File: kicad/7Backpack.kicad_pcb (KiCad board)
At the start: 2 copper layers, 14 x 83.2 mm, 14 parts, among them J1 Conn_01x06, J2 Conn_01x06, U1 TPIC6C596PWR, U2 15101BS-30101BS

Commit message: AddedGerber files
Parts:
- R9: value 30Ω ? -> 2kΩ
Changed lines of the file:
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@@
       (layerselection 0x00010fc_ffffffff)
       (disableapertmacros false)
-      (usegerberextensions false)
+      (usegerberextensions true)
       (usegerberattributes true)
       (usegerberadvancedattributes true)
-      (creategerberjobfile true)
+      (creategerberjobfile false)
       (svguseinch false)
       (svgprecision 6)
@@
       (psa4output false)
       (plotreference true)
-      (plotvalue true)
+      (plotvalue false)
       (plotinvisibletext false)
       (sketchpadsonfab false)
-      (subtractmaskfromsilk false)
+      (subtractmaskfromsilk true)
       (outputformat 1)
       (mirror false)
-      (drillshape 1)
+      (drillshape 0)
       (scaleselection 1)
-      (outputdirectory "Gerber/")
+      (outputdirectory "../Gerber/")
     )
   )
@@
     (descr "Resistor SMD 0603 (1608 Metric), square (rectangular) end terminal, IPC_7351 nominal, (Body size source: IPC-SM-782 page 72, https://www.pcb-3d.com/wordpress/wp-content/uploads/ipc-sm-782a_amendment_1_and_2.pdf), generated with kicad-footprint-generator")
     (tags "resistor")
+    (property "LCSC" "C22810")
     (property "Sheetfile" "7Backpack.kicad_sch")
     (property "Sheetname" "")
@@
     (descr "Resistor SMD 0603 (1608 Metric), square (rectangular) end terminal, IPC_7351 nominal, (Body size source: IPC-SM-782 page 72, https://www.pcb-3d.com/wordpress/wp-content/uploads/ipc-sm-782a_amendment_1_and_2.pdf), generated with kicad-footprint-generator")
     (tags "resistor")
+    (property "LCSC" "C22975")
     (property "Sheetfile" "7Backpack.kicad_sch")
     (property "Sheetname" "")
@@
       (effects (font (size 1 1) (thickness 0.15)))
     )
-    (fp_text value "30Ω ?" (at 0 1.43 90) (layer "F.Fab")
+    (fp_text value "2kΩ" (at 0 1.43 90) (layer "F.Fab")
       (effects (font (size 1 1) (thickness 0.15)))
     )
@@
     (descr "Resistor SMD 0603 (1608 Metric), square (rectangular) end terminal, IPC_7351 nominal, (Body size source: IPC-SM-782 page 72, https://www.pcb-3d.com/wordpress/wp-content/uploads/ipc-sm-782a_amendment_1_and_2.pdf), generated with kicad-footprint-generator")
     (tags "resistor")
+    (property "LCSC" "C22810")
     (property "Sheetfile" "7Backpack.kicad_sch")
     (property "Sheetname" "")
@@
     (descr "Resistor SMD 0603 (1608 Metric), square (rectangular) end terminal, IPC_7351 nominal, (Body size source: IPC-SM-782 page 72, https://www.pcb-3d.com/wordpress/wp-content/uploads/ipc-sm-782a_amendment_1_and_2.pdf), generated with kicad-footprint-generator")
     (tags "resistor")
+    (property "LCSC" "C22810")
     (property "Sheetfile" "7Backpack.kicad_sch")
     (property "Sheetname" "")
@@
     (descr "Capacitor SMD 0603 (1608 Metric), square (rectangular) end terminal, IPC_7351 nominal, (Body size source: IPC-SM-782 page 76, https://www.pcb-3d.com/wordpress/wp-content/uploads/ipc-sm-782a_amendment_1_and_2.pdf), generated with kicad-footprint-generator")
     (tags "capacitor")
+    (property "LCSC" "C14663")
     (property "Sheetfile" "7Backpack.kicad_sch")
     (property "Sheetname" "")
@@
     (descr "Resistor SMD 0603 (1608 Metric), square (rectangular) end terminal, IPC_7351 nominal, (Body size source: IPC-SM-782 page 72, https://www.pcb-3d.com/wordpress/wp-content/uploads/ipc-sm-782a_amendment_1_and_2.pdf), generated with kicad-footprint-generator")
     (tags "resistor")
+    (property "LCSC" "C22810")
     (property "Sheetfile" "7Backpack.kicad_sch")
     (property "Sheetname" "")
@@
   (footprint "TPIC6C596PWR:SOP65P640X120-16N" (layer "F.Cu")
     (at 106.68 102.87)
-    (property "Description" "\nAutomotive 8-bit shift register\n")
+    (property "LCSC" "C3304552")
     (property "MPN" "TPIC6C596PWR")
     (property "PACKAGE" "TSSOP-16")
-    (property "Package" "TSSOP-16 Texas Instruments")
     (property "Sheetfile" "7Backpack.kicad_sch")
     (property "Sheetname" "")
@@
     (descr "Resistor SMD 0603 (1608 Metric), square (rectangular) end terminal, IPC_7351 nominal, (Body size source: IPC-SM-782 page 72, https://www.pcb-3d.com/wordpress/wp-content/uploads/ipc-sm-782a_amendment_1_and_2.pdf), generated with kicad-footprint-generator")
     (tags "resistor")
+    (property "LCSC" "C25804")
     (property "Sheetfile" "7Backpack.kicad_sch")
     (property "Sheetname" "")
@@
     (descr "Resistor SMD 0603 (1608 Metric), square (rectangular) end terminal, IPC_7351 nominal, (Body size source: IPC-SM-782 page 72, https://www.pcb-3d.com/wordpress/wp-content/uploads/ipc-sm-782a_amendment_1_and_2.pdf), generated with kicad-footprint-generator")
     (tags "resistor")
+    (property "LCSC" "C22810")
     (property "Sheetfile" "7Backpack.kicad_sch")
     (property "Sheetname" "")
@@
     (descr "Resistor SMD 0603 (1608 Metric), square (rectangular) end terminal, IPC_7351 nominal, (Body size source: IPC-SM-782 page 72, https://www.pcb-3d.com/wordpress/wp-content/uploads/ipc-sm-782a_amendment_1_and_2.pdf), generated with kicad-footprint-generator")
     (tags "resistor")
+    (property "LCSC" "C22810")
     (property "Sheetfile" "7Backpack.kicad_sch")
     (property "Sheetname" "")
@@
     (descr "Resistor SMD 0603 (1608 Metric), square (rectangular) end terminal, IPC_7351 nominal, (Body size source: IPC-SM-782 page 72, https://www.pcb-3d.com/wordpress/wp-content/uploads/ipc-sm-782a_amendment_1_and_2.pdf), generated with kicad-footprint-generator")
     (tags "resistor")
-    (property "Sheetfile" "7Backpack.kicad_sch")
-    (property "Sheetname" "")
+    (property "LCSC" "C22810")
+    (property "Sheetfile" "7Backpack.kicad_sch")
+    (property "Sheetname" "")

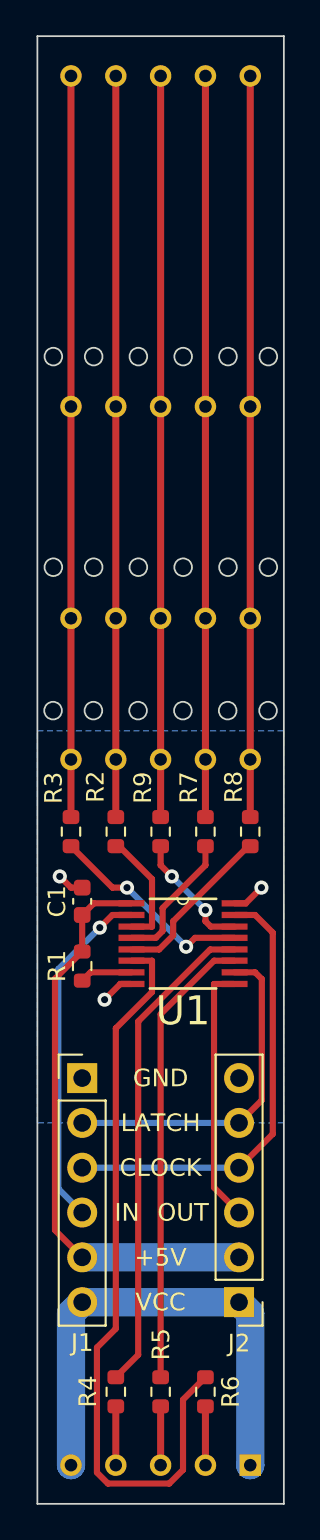
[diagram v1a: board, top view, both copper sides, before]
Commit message: Switched to SOP-16
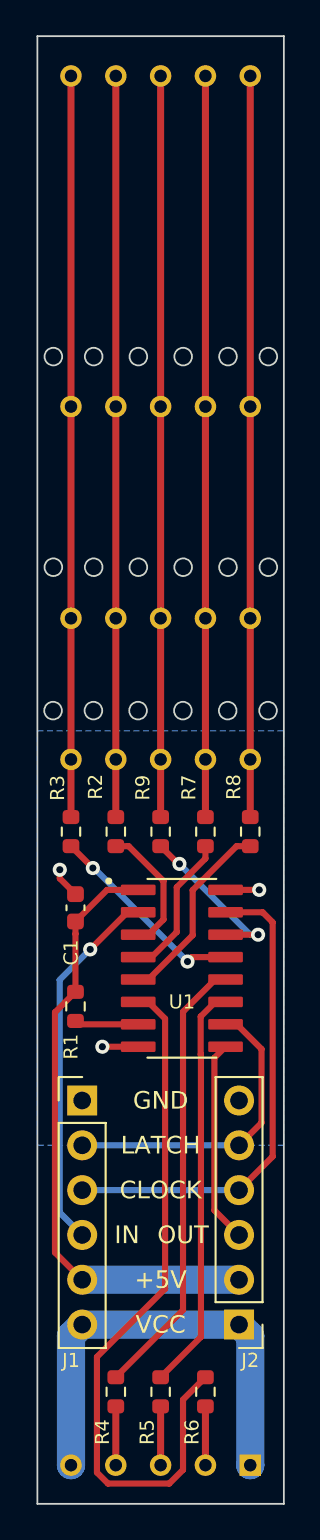
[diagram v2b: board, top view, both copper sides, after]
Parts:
- R1: value 10kΩ -> 10k
- R2, R3, R4, R5, R6, R7, R8: value 15Ω -> 15
- R9: value 2kΩ -> 2k
- U1: value TPIC6C596PWR -> TPIC6C596DC; footprint TPIC6C596PWR:SOP65P640X120-16N -> TPIC6C596DR:SOIC127P600X175-16N
- moved R1 2.32 mm to (100.6, 106.4)
- moved U1 1.40 mm to (106.6, 104.3)
- moved J1 1.27 mm to (101.0, 111.8)
- moved J2 1.27 mm to (109.9, 124.5)
- moved C1 0.53 mm to (100.6, 100.8)
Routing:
- net Net-(J2-Pad3): track 14.7 -> 11.5 mm
- net Net-(R5-Pad1): track 26.0 -> 23.2 mm
- net VCC: track 27.9 -> 25.4 mm
- net Net-(R4-Pad1): track 27.8 -> 25.5 mm
- net Net-(R9-Pad1): track 7.08 -> 9.45 mm
- net Net-(R6-Pad1): track 42.7 -> 40.5 mm
- net Net-(J1-Pad3): track 25.6 -> 27.8 mm
- net +5V: track 32.6 -> 34.6 mm
- net Net-(J1-Pad2): track 19.3 -> 17.5 mm
- net Net-(J1-Pad4): track 19.8 -> 21.0 mm
- net Net-(R8-Pad1): track 9.82 -> 11.0 mm
- net Net-(R2-Pad1): track 6.68 -> 7.49 mm
- net Net-(R1-Pad1): track 2.99 -> 3.64 mm
- net Net-(R7-Pad1): track 7.74 -> 8.31 mm
